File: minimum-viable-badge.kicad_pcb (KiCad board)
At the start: 2 copper layers, 100 x 64 mm, 46 parts, among them P1 BATTERY, P10 POT_4, P11 MECH, P12 MECH, P13 MECH, P2 USB, P4 eInk, P6 POT_1, P7 POT_2, P9 POT_3, Q1 S8050, Q2 S8050, SW3 ON|OFF, U1 CP2102, U2 ESP32-WROOM, U3 NCP5501, U4 MCP73831

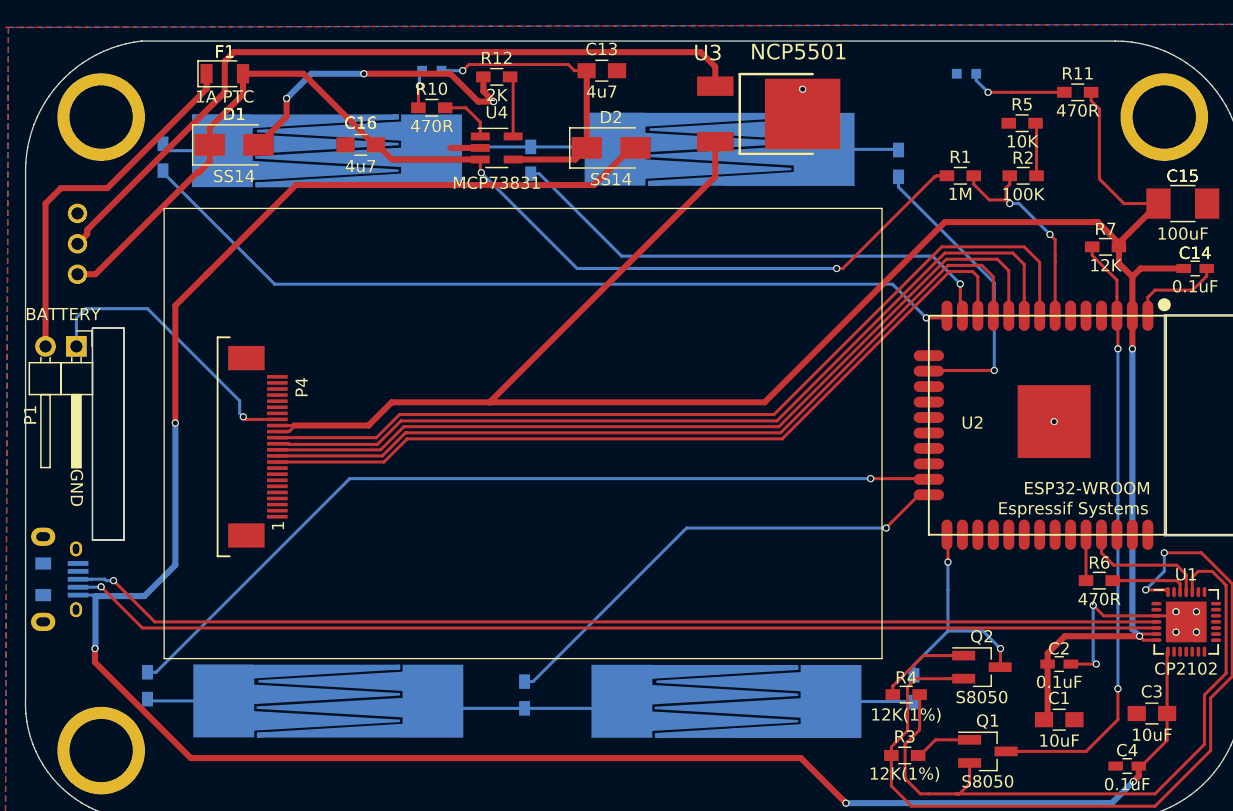
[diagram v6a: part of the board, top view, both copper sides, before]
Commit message: updated touch sensors
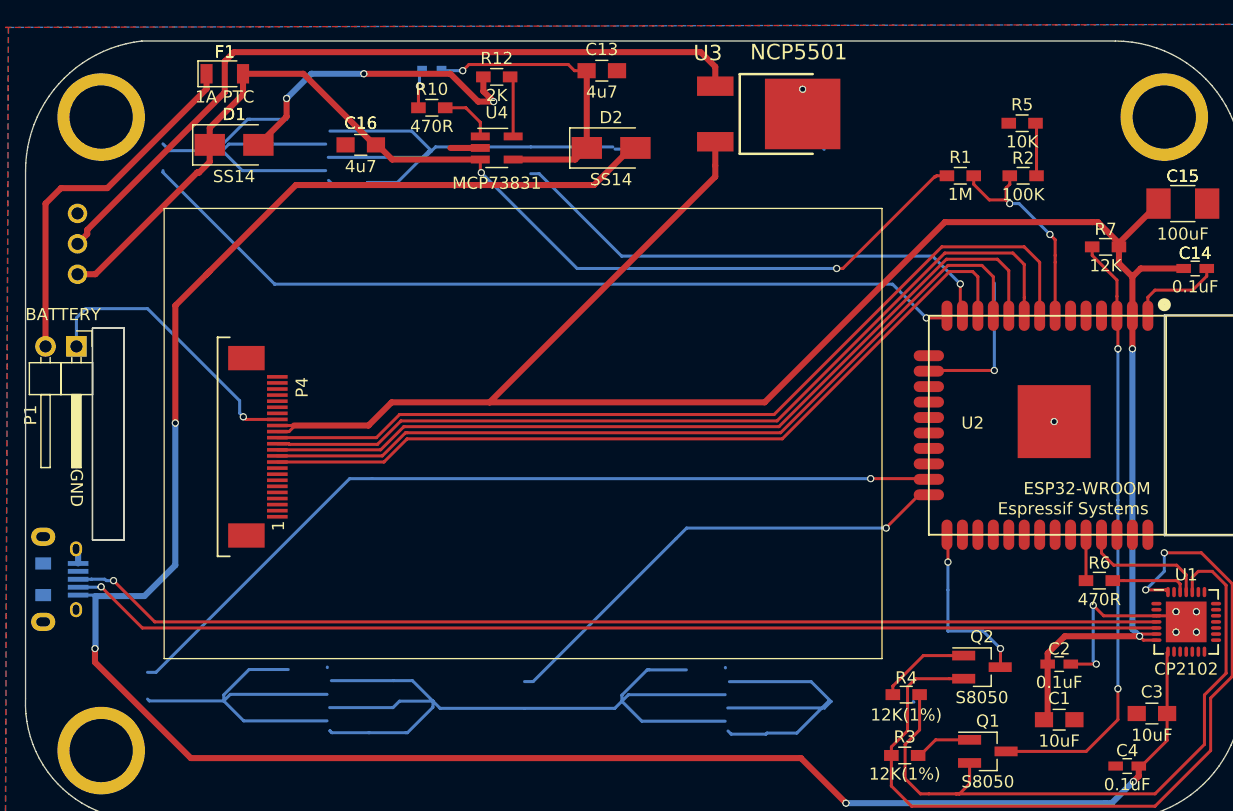
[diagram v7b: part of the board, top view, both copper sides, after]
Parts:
- removed D4: POWER, LEDs:LED_0603
- removed P10: POT_4, libs:sense_pot
- removed P6: POT_1, libs:sense_pot
- removed P7: POT_2, libs:sense_pot
- removed P9: POT_3, libs:sense_pot
- removed R11: 470R, Resistors_SMD:R_0603_HandSoldering
- removed R13, R14, R16, R17, R18, R20: 100, Resistors_SMD:R_0603_HandSoldering
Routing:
- net Net-(P7-Pad2): track 33.6 -> 2.31 mm
- net Net-(P6-Pad2): track 70.6 -> 45.2 mm
- net +3V3: track 179.9 -> 166.8 mm
- net /IO13: track 24.6 -> 12.6 mm
- net Net-(D4-Pad2): track 8.20 -> 0.00 mm, vias 1 -> 0
- net Net-(P10-Pad2): track 34.3 -> 27.5 mm
- net /IO0: track 19.2 -> 14.4 mm
- net GND: track 74.6 -> 75.8 mm

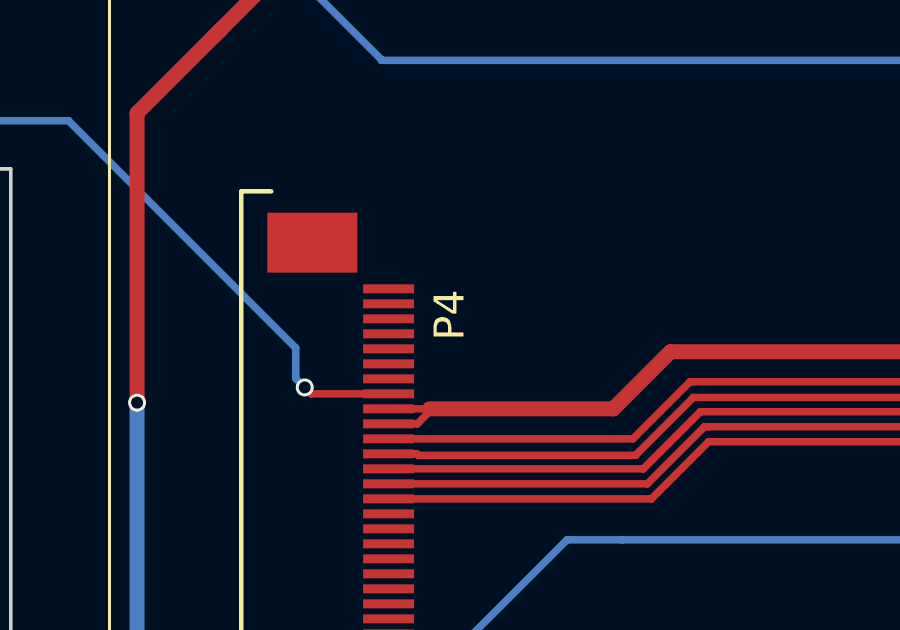
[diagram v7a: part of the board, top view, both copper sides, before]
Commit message: Add e-ink gate drive circuitry
Closes #14
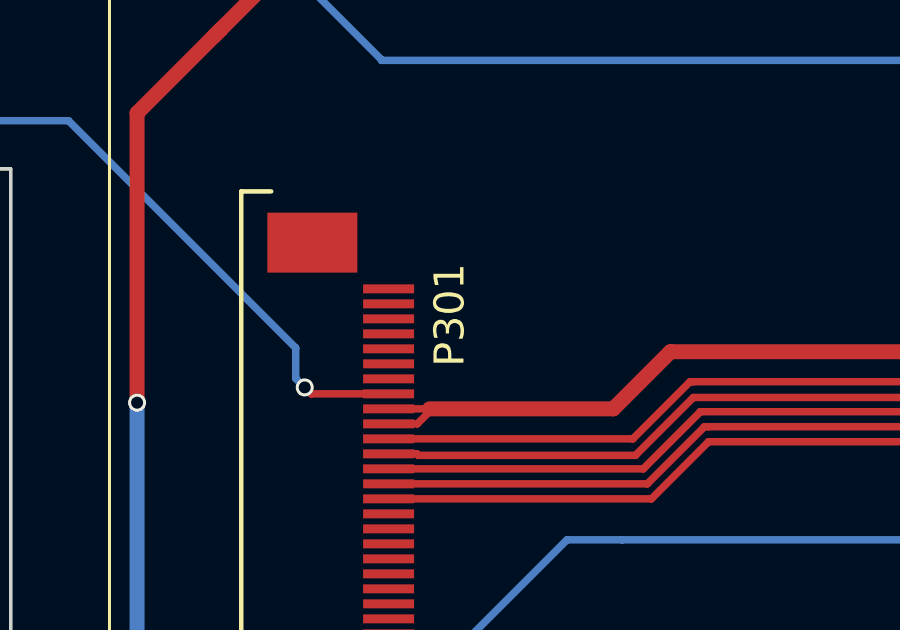
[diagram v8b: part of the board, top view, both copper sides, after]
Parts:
- renumbered P4 to P301
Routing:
- net (no net): track 0.00 -> 203.8 mm
- net Net-(P10-Pad1): track 68.3 -> 0.00 mm
- net Net-(P6-Pad2): track 45.2 -> 0.00 mm
- net Net-(P9-Pad1): track 30.9 -> 0.00 mm
- net Net-(P6-Pad1): track 29.7 -> 0.00 mm
- net Net-(P10-Pad2): track 27.5 -> 0.00 mm
- net Net-(P7-Pad2): track 2.31 -> 0.00 mm
